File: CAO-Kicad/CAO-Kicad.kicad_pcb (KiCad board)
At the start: 2 copper layers, 100 x 100 mm, 3 parts, among them J1 Conn_01x02

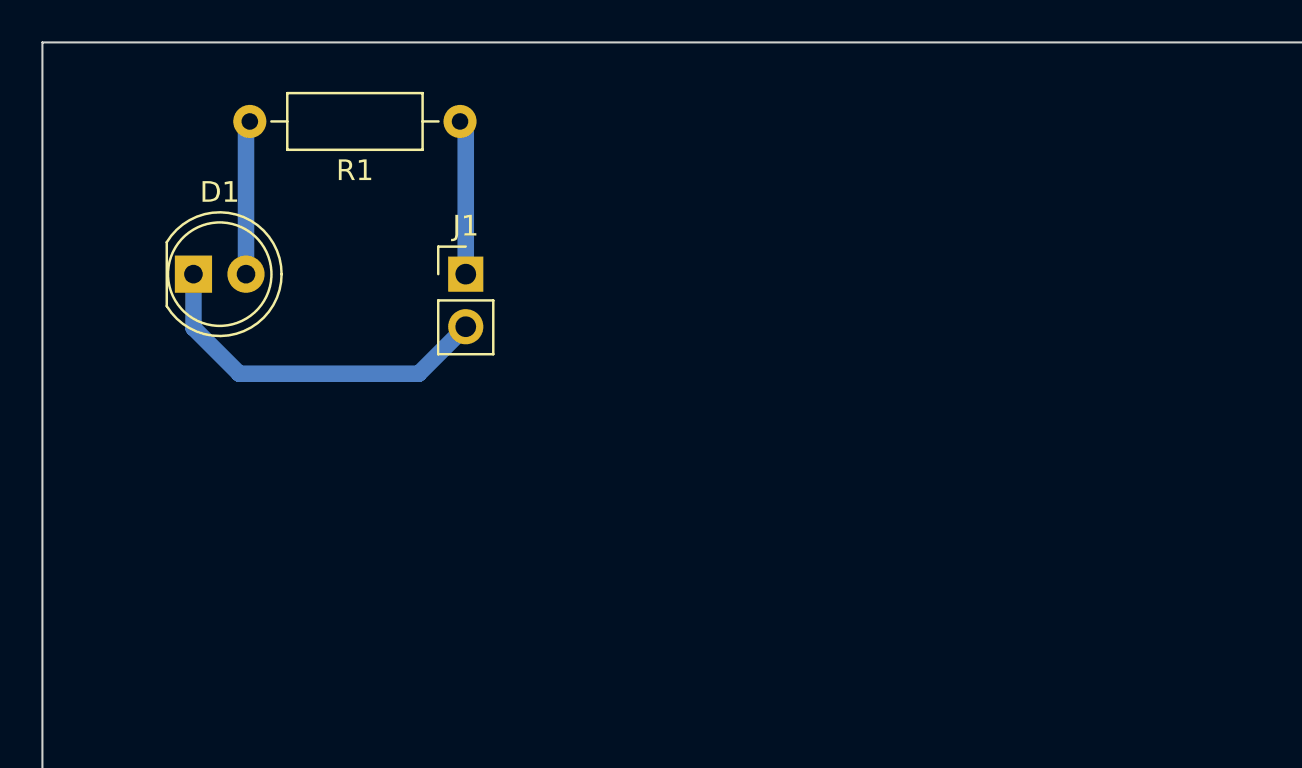
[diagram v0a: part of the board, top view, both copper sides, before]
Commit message: Ajout du conn ICSP et du contour de carte 100x100mm
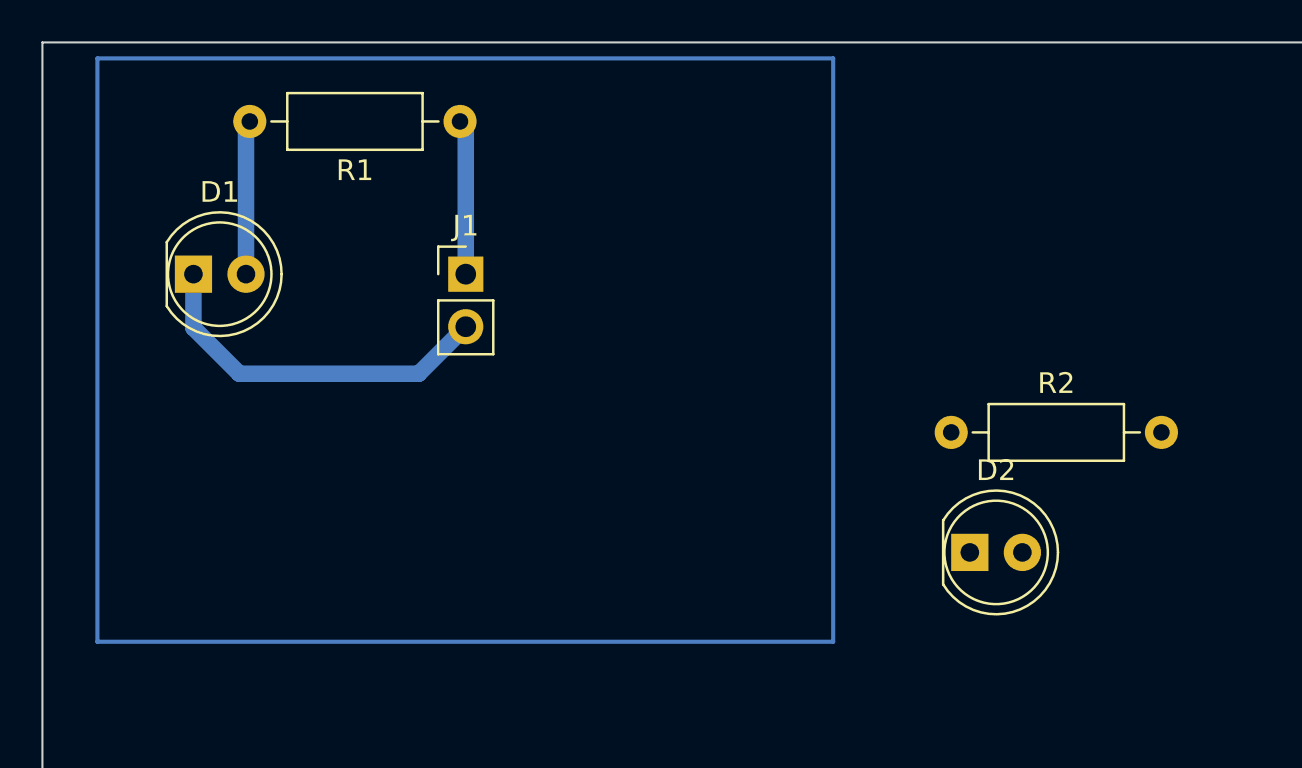
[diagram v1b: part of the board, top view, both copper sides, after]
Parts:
- added D2: LED, LED_THT:LED_D5.0mm, F.Cu at (99.8, 104.6)
- added R2: R, Resistor_THT:R_Axial_DIN0207_L6.3mm_D2.5mm_P10.16mm_Horizontal, F.Cu at (98.9, 98.8)
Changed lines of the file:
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@@
   (net 2 "Net-(D1-Pad2)")
   (net 3 "Net-(J1-Pad1)")
+  (net 4 "unconnected-(D2-Pad1)")
+  (net 5 "Net-(D2-Pad2)")
+  (net 6 "unconnected-(R2-Pad1)")
   (footprint "Resistor_THT:R_Axial_DIN0207_L6.3mm_D2.5mm_P10.16mm_Horizontal" (layer "F.Cu")
     (at 75.184 83.82 180)
@@
     (fp_line (start 8.23 -1.25) (end 1.93 -1.25) (layer "F.Fab") (width 0.1))
     (pad "1" thru_hole circle locked (at 0 0 180) (size 1.6 1.6) (drill 0.8) (layers *.Cu *.Mask)
-      (net 3 "Net-(J1-Pad1)"))
+      (net 3 "Net-(J1-Pad1)") (pintype "passive"))
     (pad "2" thru_hole oval locked (at 10.16 0 180) (size 1.6 1.6) (drill 0.8) (layers *.Cu *.Mask)
-      (net 2 "Net-(D1-Pad2)"))
+      (net 2 "Net-(D1-Pad2)") (pintype "passive"))
     (model "${KICAD6_3DMODEL_DIR}/Resistor_THT.3dshapes/R_Axial_DIN0207_L6.3mm_D2.5mm_P10.16mm_Horizontal.wrl"
       (offset (xyz 0 0 0))
@@
     (fp_circle (center 1.27 0) (end 3.77 0) (layer "F.Fab") (width 0.1) (fill none))
     (pad "1" thru_hole rect locked (at 0 0) (size 1.8 1.8) (drill 0.9) (layers *.Cu *.Mask)
-      (net 1 "Net-(D1-Pad1)") (pinfunction "K"))
+      (net 1 "Net-(D1-Pad1)") (pinfunction "K") (pintype "passive"))
     (pad "2" thru_hole circle locked (at 2.54 0) (size 1.8 1.8) (drill 0.9) (layers *.Cu *.Mask)
-      (net 2 "Net-(D1-Pad2)") (pinfunction "A"))
+      (net 2 "Net-(D1-Pad2)") (pinfunction "A") (pintype "passive"))
     (model "${KICAD6_3DMODEL_DIR}/LED_THT.3dshapes/LED_D5.0mm.wrl"
       (offset (xyz 0 0 0))
@@
     (fp_line (start 1.27 -1.27) (end 1.27 3.81) (layer "F.Fab") (width 0.1))
     (pad "1" thru_hole rect locked (at 0 0) (size 1.7 1.7) (drill 1) (layers *.Cu *.Mask)
-      (net 3 "Net-(J1-Pad1)") (pinfunction "Pin_1"))
+      (net 3 "Net-(J1-Pad1)") (pinfunction "Pin_1") (pintype "passive"))
     (pad "2" thru_hole oval locked (at 0 2.54) (size 1.7 1.7) (drill 1) (layers *.Cu *.Mask)
-      (net 1 "Net-(D1-Pad1)") (pinfunction "Pin_2"))
+      (net 1 "Net-(D1-Pad1)") (pinfunction "Pin_2") (pintype "passive"))
     (model "${KICAD6_3DMODEL_DIR}/Connector_PinHeader_2.54mm.3dshapes/PinHeader_1x02_P2.54mm_Vertical.wrl"
       (offset (xyz 0 0 0))
@@
     )
   )
+  (footprint "Resistor_THT:R_Axial_DIN0207_L6.3mm_D2.5mm_P10.16mm_Horizontal" (layer "F.Cu")
+    (at 98.922 98.848)
+    (descr "Resistor, Axial_DIN0207 series, Axial, Horizontal, pin pitch=10.16mm, 0.25W = 1/4W, length*diameter=6.3*2.5mm^2, http://cdn-reichelt.de/documents/datenblatt/B400/1_4W%23YAG.pdf")
+    (tags "Resistor Axial_DIN0207 series Axial Horizontal pin pitch 10.16mm 0.25W = 1/4W length 6.3mm diameter 2.5mm")
+    (property "Sheetfile" "CAO-Kicad.kicad_sch")
+    (property "Sheetname" "")
+    (attr through_hole)
+    (fp_text reference "R2" (at 5.08 -2.37) (layer "F.SilkS")
+      (effects (font (size 1 1) (thickness 0.15)))
+    )
+    (fp_text value "R" (at 5.08 2.37) (layer "F.Fab")
+      (effects (font (size 1 1) (thickness 0.15)))
+    )
+    (fp_text user "${REFERENCE}" (at 5.08 0) (layer "F.Fab")
+      (effects (font (size 1 1) (thickness 0.15)))
+    )
+    (fp_line (start 9.12 0) (end 8.35 0) (layer "F.SilkS") (width 0.12))
+    (fp_line (start 1.81 -1.37) (end 1.81 1.37) (layer "F.SilkS") (width 0.12))
+    (fp_line (start 8.35 1.37) (end 8.35 -1.37) (layer "F.SilkS") (width 0.12))
+    (fp_line (start 1.81 1.37) (end 8.35 1.37) (layer "F.SilkS") (width 0.12))
+    (fp_line (start 8.35 -1.37) (end 1.81 -1.37) (layer "F.SilkS") (width 0.12))
+    (fp_line (start 1.04 0) (end 1.81 0) (layer "F.SilkS") (width 0.12))
+    (fp_line (start 11.21 -1.5) (end -1.05 -1.5) (layer "F.CrtYd") (width 0.05))
+    (fp_line (start 11.21 1.5) (end 11.21 -1.5) (layer "F.CrtYd") (width 0.05))
+    (fp_line (start -1.05 1.5) (end 11.21 1.5) (layer "F.CrtYd") (width 0.05))
+    (fp_line (start -1.05 -1.5) (end -1.05 1.5) (layer "F.CrtYd") (width 0.05))
+    (fp_line (start 0 0) (end 1.93 0) (layer "F.Fab") (width 0.1))
+    (fp_line (start 8.23 -1.25) (end 1.93 -1.25) (layer "F.Fab") (width 0.1))
+    (fp_line (start 8.23 1.25) (end 8.23 -1.25) (layer "F.Fab") (width 0.1))
+    (fp_line (start 1.93 -1.25) (end 1.93 1.25) (layer "F.Fab") (width 0.1))
+    (fp_line (start 1.93 1.25) (end 8.23 1.25) (layer "F.Fab") (width 0.1))
+    (fp_line (start 10.16 0) (end 8.23 0) (layer "F.Fab") (width 0.1))
+    (pad "1" thru_hole circle locked (at 0 0) (size 1.6 1.6) (drill 0.8) (layers *.Cu *.Mask)
+      (net 6 "unconnected-(R2-Pad1)") (pintype "passive"))
+    (pad "2" thru_hole oval locked (at 10.16 0) (size 1.6 1.6) (drill 0.8) (layers *.Cu *.Mask)
+      (net 5 "Net-(D2-Pad2)") (pintype "passive"))
+    (model "${KICAD6_3DMODEL_DIR}/Resistor_THT.3dshapes/R_Axial_DIN0207_L6.3mm_D2.5mm_P10.16mm_Horizontal.wrl"
+      (offset (xyz 0 0 0))
+      (scale (xyz 1 1 1))
+      (rotate (xyz 0 0 0))
+    )
+  )
+  (footprint "LED_THT:LED_D5.0mm" (layer "F.Cu")
+    (at 99.822 104.648)
+    (descr "LED, diameter 5.0mm, 2 pins, http://cdn-reichelt.de/documents/datenblatt/A500/LL-504BC2E-009.pdf")
+    (tags "LED diameter 5.0mm 2 pins")
+    (property "Sheetfile" "CAO-Kicad.kicad_sch")
+    (property "Sheetname" "")
+    (attr through_hole)
+    (fp_text reference "D2" (at 1.27 -3.96) (layer "F.SilkS")
+      (effects (font (size 1 1) (thickness 0.15)))
+    )
+    (fp_text value "LED" (at 1.27 3.96) (layer "F.Fab")
+      (effects (font (size 1 1) (thickness 0.15)))
+    )
+    (fp_text user "${REFERENCE}" (at 1.25 0) (layer "F.Fab")
+      (effects (font (size 0.8 0.8) (thickness 0.2)))
+    )
+    (fp_line (start -1.29 -1.545) (end -1.29 1.545) (layer "F.SilkS") (width 0.12))
+    (fp_arc (start 1.27 0) (end -1.29 -1.54483) (angle 148.9) (layer "F.SilkS") (width 0.12))
+    (fp_arc (start 1.27 0) (end -1.29 1.54483) (angle -148.9) (layer "F.SilkS") (width 0.12))
+    (fp_circle (center 1.27 0) (end 3.77 0) (layer "F.SilkS") (width 0.12) (fill none))
+    (fp_line (start -1.95 -3.25) (end -1.95 3.25) (layer "F.CrtYd") (width 0.05))
+    (fp_line (start -1.95 3.25) (end 4.5 3.25) (layer "F.CrtYd") (width 0.05))
+    (fp_line (start 4.5 -3.25) (end -1.95 -3.25) (layer "F.CrtYd") (width 0.05))
+    (fp_line (start 4.5 3.25) (end 4.5 -3.25) (layer "F.CrtYd") (width 0.05))
+    (fp_line (start -1.23 -1.469694) (end -1.23 1.469694) (layer "F.Fab") (width 0.1))
+    (fp_arc (start 1.27 0) (end -1.23 -1.469694) (angle 299.1) (layer "F.Fab") (width 0.1))
+    (fp_circle (center 1.27 0) (end 3.77 0) (layer "F.Fab") (width 0.1) (fill none))
+    (pad "1" thru_hole rect locked (at 0 0) (size 1.8 1.8) (drill 0.9) (layers *.Cu *.Mask)
+      (net 4 "unconnected-(D2-Pad1)") (pinfunction "K") (pintype "passive"))
+    (pad "2" thru_hole circle locked (at 2.54 0) (size 1.8 1.8) (drill 0.9) (layers *.Cu *.Mask)
+      (net 5 "Net-(D2-Pad2)") (pinfunction "A") (pintype "passive"))
+    (model "${KICAD6_3DMODEL_DIR}/LED_THT.3dshapes/LED_D5.0mm.wrl"
+      (offset (xyz 0 0 0))
+      (scale (xyz 1 1 1))
+      (rotate (xyz 0 0 0))
+    )
+  )
+  (gr_rect (start 57.658 80.772) (end 93.218 108.966) (layer "B.Cu") (width 0.2) (fill none))
   (gr_line (start 55 180) (end 55 80) (layer "Edge.Cuts") (width 0.1))
   (gr_line (start 55 80) (end 155 80) (layer "Edge.Cuts") (width 0.1))

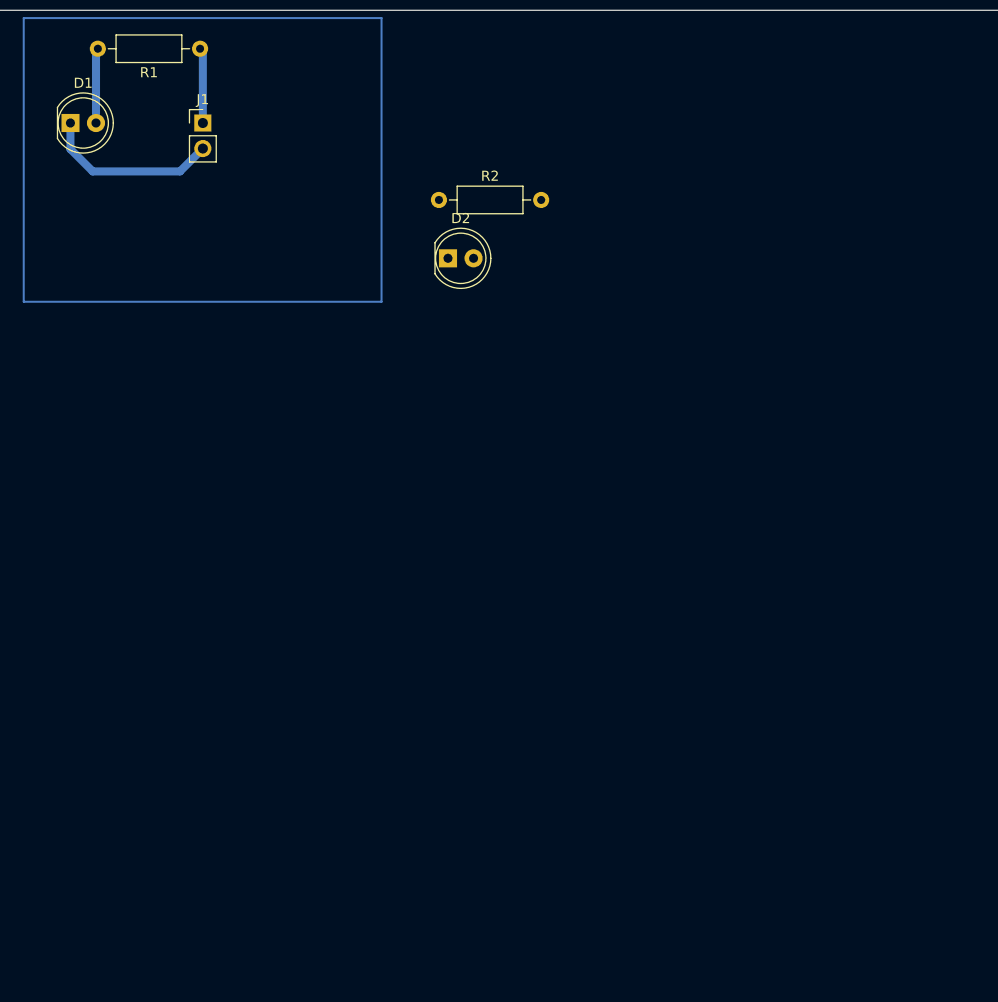
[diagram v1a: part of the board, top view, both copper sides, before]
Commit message: Ajout de la serigraphie et recherche composants
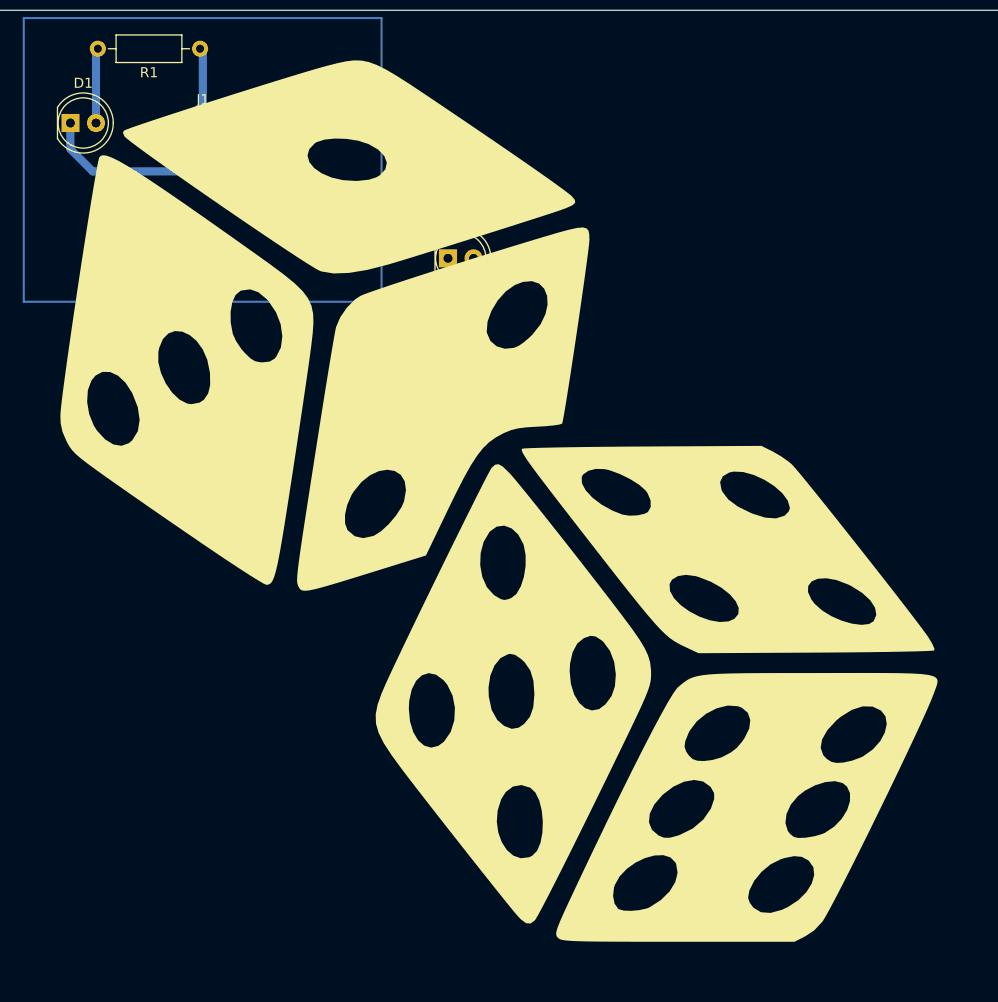
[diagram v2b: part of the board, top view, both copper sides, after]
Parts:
- added G***: LOGO, Image:image_de, F.Cu at (104.9, 128.8)

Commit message: Ajout des docs et images
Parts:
- moved G*** 55.9 mm to (146.3, 91.2)
- moved D1 55.9 mm to (103.3, 53.2)
- moved D2 55.9 mm to (140.8, 66.6)
- moved J1 55.9 mm to (116.5, 53.2)
- moved R2 55.9 mm to (139.9, 60.8)
- moved R1 55.9 mm to (116.2, 45.8)
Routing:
- net Net-(D1-Pad1): track 17.6 -> 0.00 mm
- net Net-(J1-Pad1): track 7.49 -> 0.00 mm
- added copper zone on B.Cu, net (none)

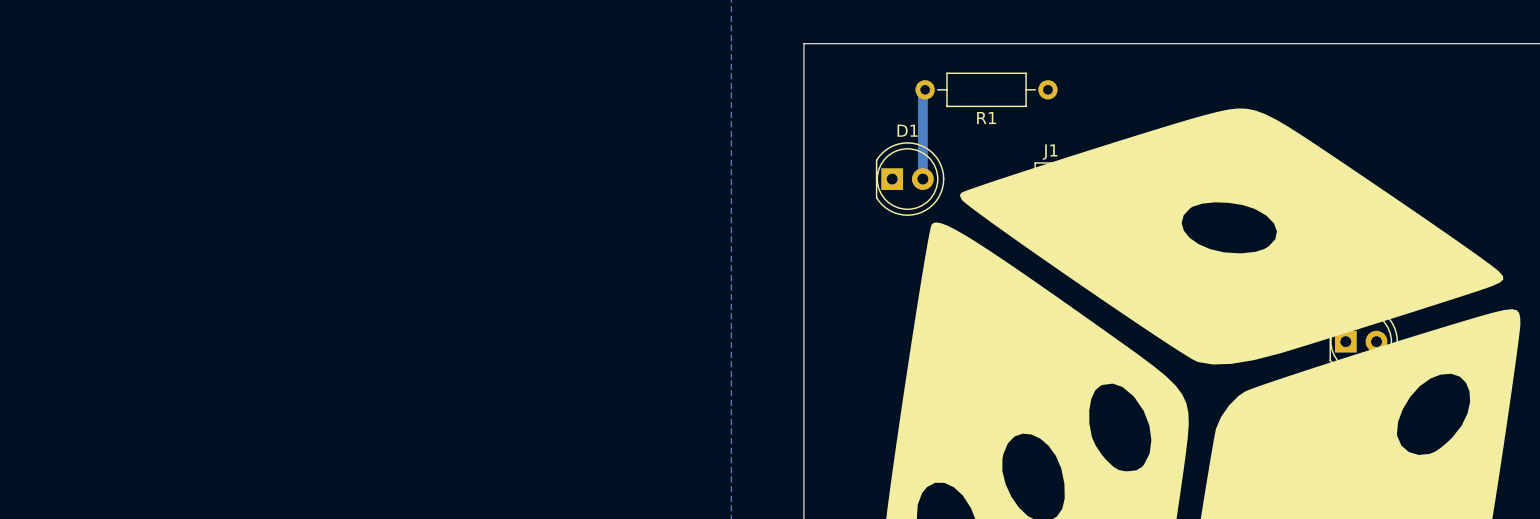
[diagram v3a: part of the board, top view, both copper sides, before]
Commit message: Importation des composants vers le circuit imprimé
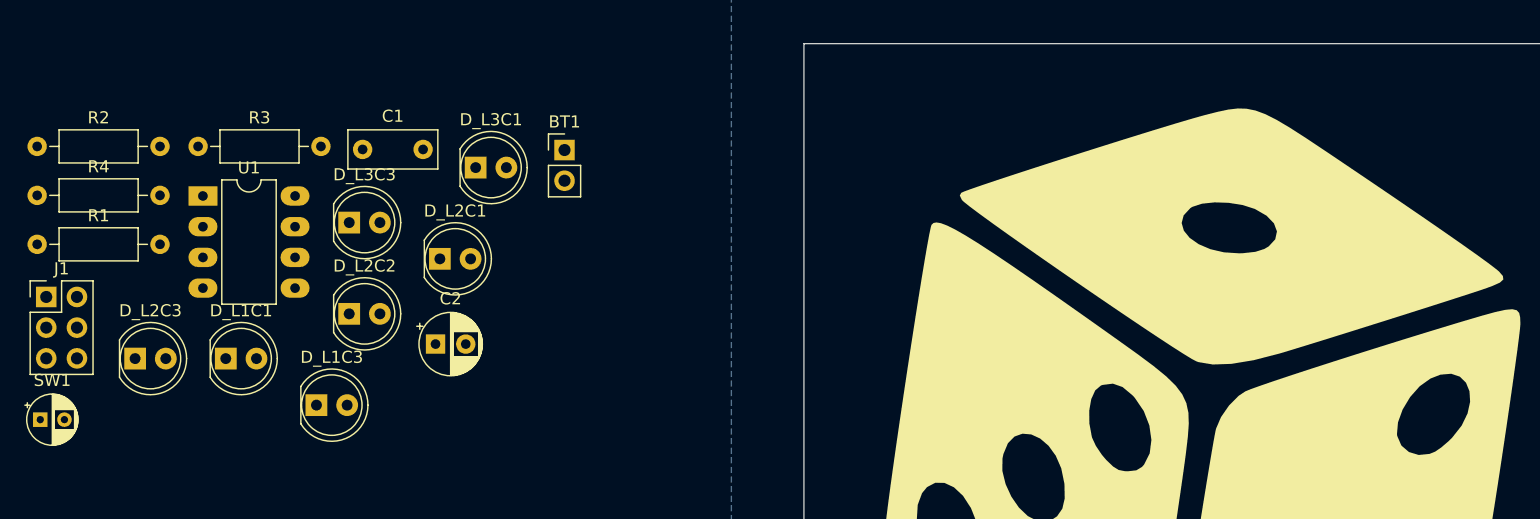
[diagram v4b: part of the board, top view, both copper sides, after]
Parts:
- removed D1, D2: LED, LED_THT:LED_D5.0mm
- added BT1: Battery_Cell_3V, Connector_PinHeader_2.54mm:PinHeader_1x02_P2.54mm_Vertical, F.Cu at (76.2, 50.8)
- added C1: 100n, Capacitor_THT:C_Rect_L7.2mm_W3.0mm_P5.00mm_FKS2_FKP2_MKS2_MKP2, F.Cu at (59.5, 50.8)
- added C2: 10u, Capacitor_THT:CP_Radial_D5.0mm_P2.50mm, F.Cu at (65.5, 66.8)
- added D_L1C1: LED, LED_THT:LED_D5.0mm_Clear, F.Cu at (48.2, 68.0)
- added D_L1C3: LED, LED_THT:LED_D5.0mm_Clear, F.Cu at (55.7, 71.9)
- added D_L2C1: LED, LED_THT:LED_D5.0mm_Clear, F.Cu at (65.9, 59.8)
- added D_L2C2: LED, LED_THT:LED_D5.0mm_Clear, F.Cu at (58.4, 64.3)
- added D_L2C3: LED, LED_THT:LED_D5.0mm_Clear, F.Cu at (40.7, 68.0)
- added D_L3C1: LED, LED_THT:LED_D5.0mm_Clear, F.Cu at (68.8, 52.2)
- added D_L3C3: LED, LED_THT:LED_D5.0mm_Clear, F.Cu at (58.4, 56.8)
- added R3: 560, Resistor_THT:R_Axial_DIN0207_L6.3mm_D2.5mm_P10.16mm_Horizontal, F.Cu at (45.9, 50.5)
- added R4: 560, Resistor_THT:R_Axial_DIN0207_L6.3mm_D2.5mm_P10.16mm_Horizontal, F.Cu at (32.6, 54.5)
- added SW1: COMMUTATEUR A BILLE, Capacitor_THT:CP_Radial_D4.0mm_P2.00mm, F.Cu at (32.8, 73.1)
- added U1: ATtiny85V-10P, Package_DIP:DIP-8_W7.62mm_LongPads, F.Cu at (46.3, 54.6)
- J1: value Conn_01x02 -> ICSP; footprint Connector_PinHeader_2.54mm:PinHeader_1x02_P2.54mm_Vertical -> Connector_PinHeader_2.54mm:PinHeader_2x03_P2.54mm_Vertical
- R1: value R -> 1k
- R2: value R -> 560
- moved R2 107.8 mm to (32.6, 50.5)
- moved R1 84.6 mm to (32.6, 58.6), turned to 0 degrees
- moved J1 83.7 mm to (33.3, 63.0)
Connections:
- J1 pad 1: Net-(J1-Pad1) -> /De electronique/PB1/MISO
- J1 pad 2: Net-(D1-Pad1) -> VCC
- R1 pad 1: Net-(J1-Pad1) -> /De electronique/CMD_L2C2
- R1 pad 2: Net-(D1-Pad2) -> /De electronique/D_L2C2
- R2 pad 1: unconnected-(R2-Pad1) -> /De electronique/PB1/MISO
- R2 pad 2: Net-(D2-Pad2) -> /De electronique/D_L3C1L1C3
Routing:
- net Net-(D1-Pad2): track 7.46 -> 0.00 mm
